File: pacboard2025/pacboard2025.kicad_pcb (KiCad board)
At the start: 4 copper layers, 80 x 85 mm, 30 parts, among them J1 XT30 Male Connector, U1 NMOS, U2 D24V50F5, U3 ProS3

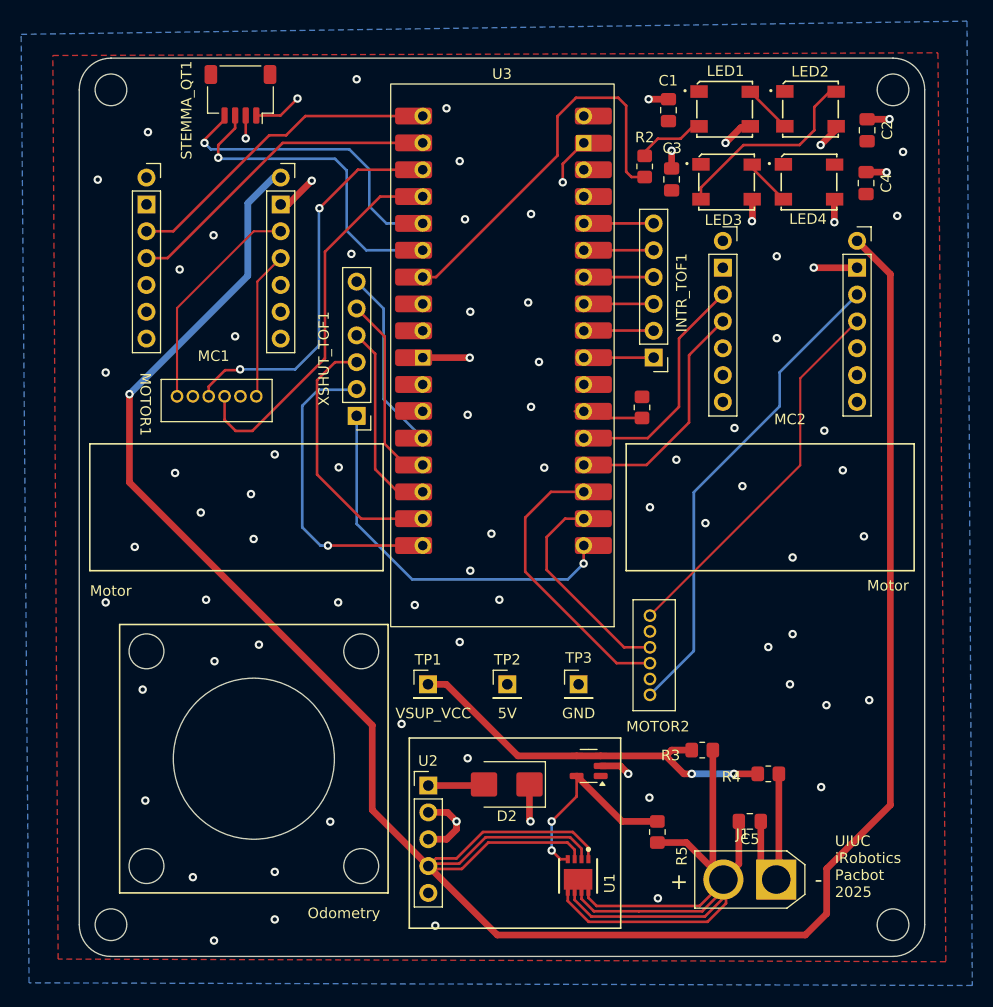
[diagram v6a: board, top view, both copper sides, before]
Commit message: final changes, pcb ordered
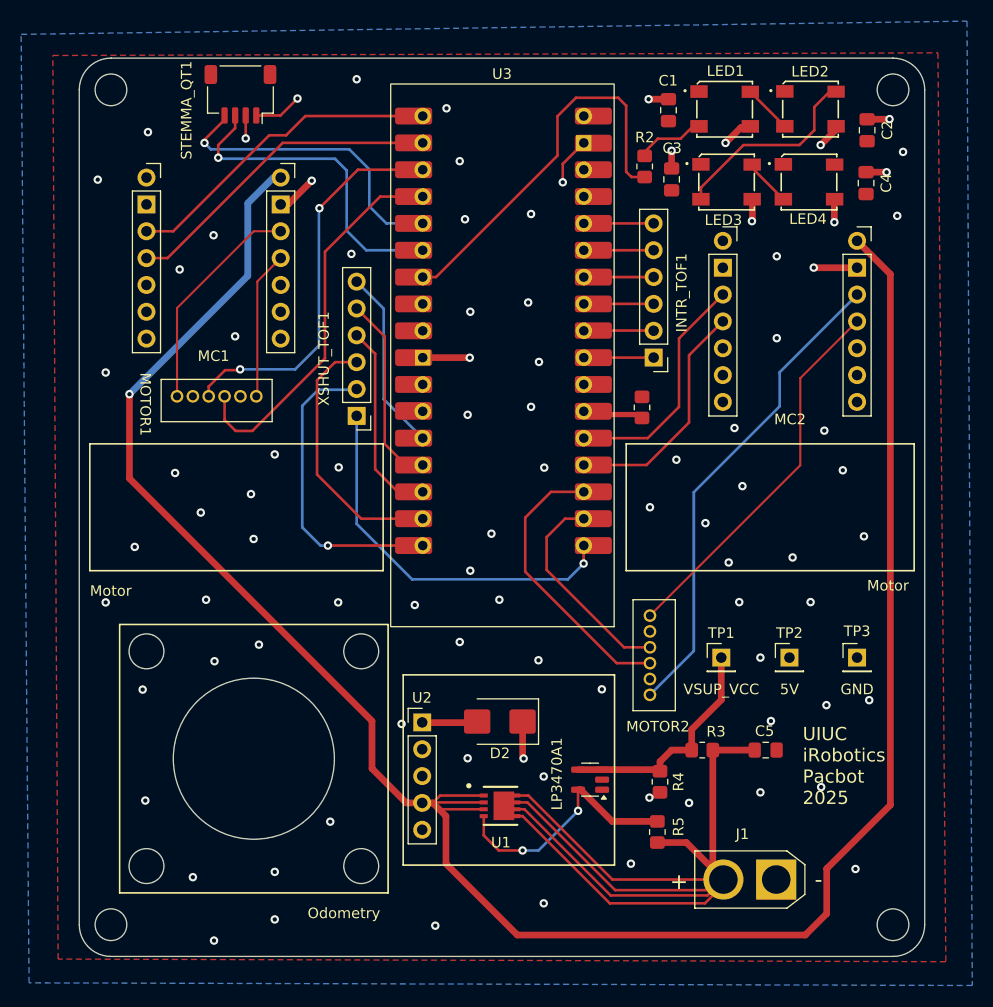
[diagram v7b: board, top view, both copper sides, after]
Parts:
- moved TP1 27.9 mm to (172.3, 118.0)
- moved TP2 26.8 mm to (178.8, 118.0)
- moved TP3 26.5 mm to (185.2, 118.0)
- moved R4 10.3 mm to (166.5, 129.8), turned to -90 degrees
- moved U1 9.89 mm to (151.4, 132.0), turned to 0 degrees
- moved C5 6.91 mm to (176.5, 126.8)
- moved U2 6.00 mm to (144.0, 124.1)
- moved D2 5.99 mm to (151.3, 124.0)
- moved LP3470A1 1.31 mm to (159.9, 129.6)
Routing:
- net /12V: track 243.3 -> 208.3 mm
- net /BAT_12V: track 95.1 -> 119.7 mm, vias 1 -> 0
- net /GND: track 50.0 -> 26.5 mm, vias 72 -> 80
- net Net-(LP3470A1-VCC): track 37.4 -> 22.0 mm, vias 2 -> 0
- net Net-(LP3470A1-RESET): track 19.3 -> 23.6 mm
